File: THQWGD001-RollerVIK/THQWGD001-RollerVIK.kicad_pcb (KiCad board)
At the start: 2 copper layers, 32.1 x 32.1 mm, 9 parts, among them J1 vik-module-connector, J2 Conn_01x02, J3 Conn_01x03

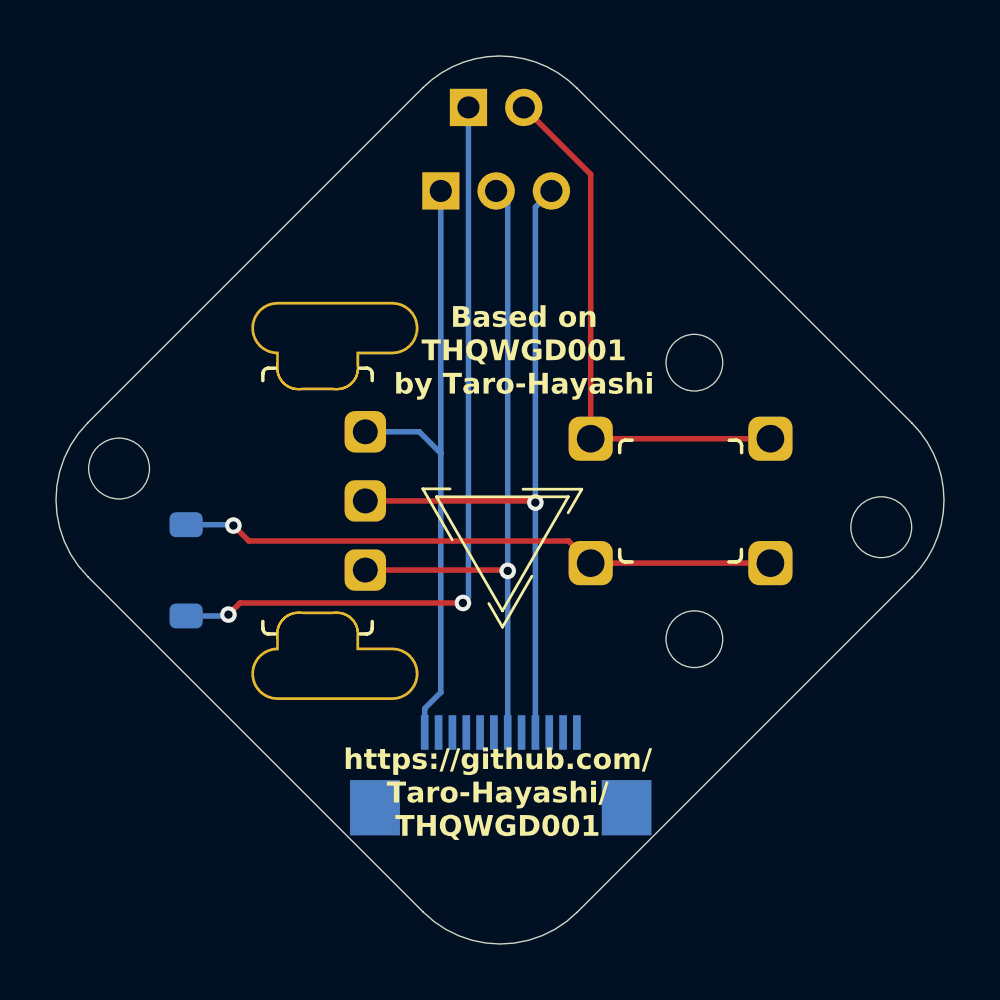
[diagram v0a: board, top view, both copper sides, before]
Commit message: Adjusted the diode placement
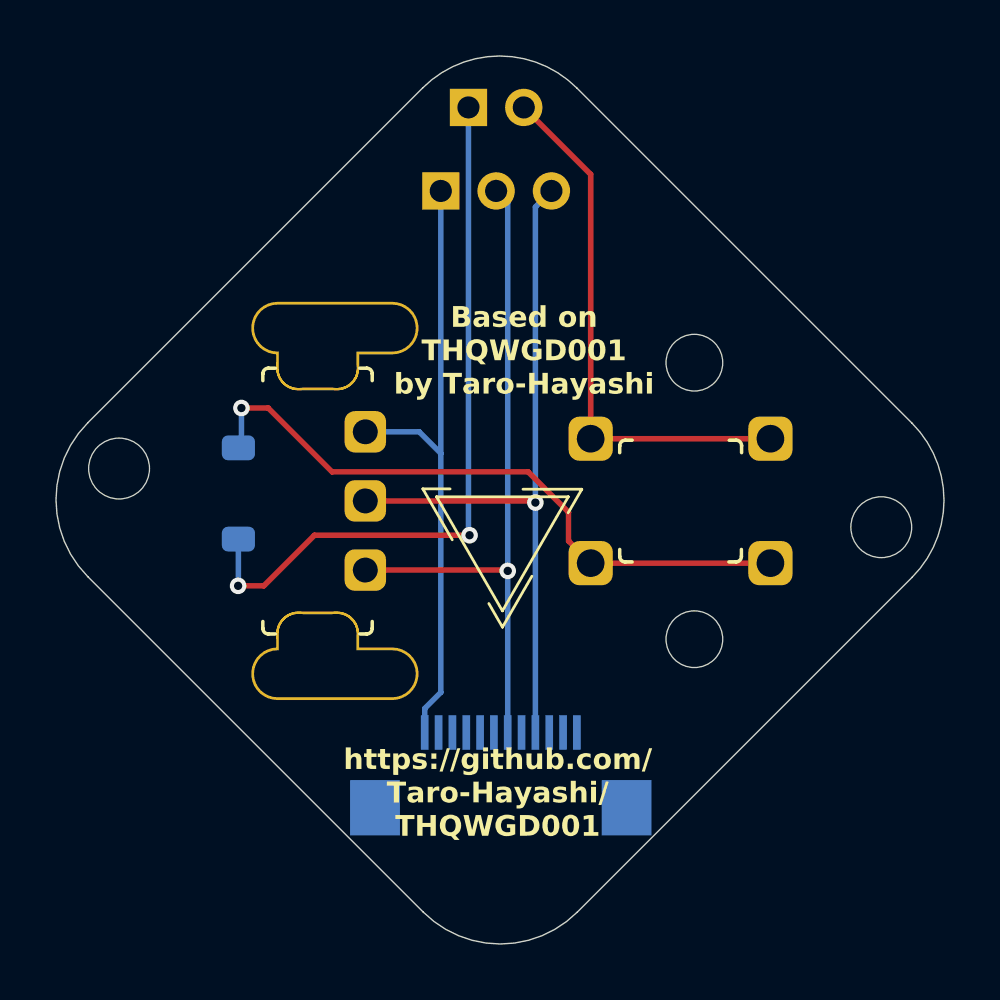
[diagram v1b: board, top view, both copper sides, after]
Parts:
- moved D1 3.36 mm to (116.9, 83.8)
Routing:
- net ROW: track 28.2 -> 26.3 mm
- net Net-(D1-A): track 21.7 -> 23.5 mm
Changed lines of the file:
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@@
 			(fill no)
 			(layer "Cmts.User")
-			(net 11)
 		)
 		(fp_circle
@@
 			(fill no)
 			(layer "F.CrtYd")
-			(net 11)
 		)
 		(fp_text user "${REFERENCE}"
@@
 			(fill no)
 			(layer "Cmts.User")
-			(net 11)
 		)
 		(fp_circle
@@
 			(fill no)
 			(layer "F.CrtYd")
-			(net 11)
 		)
 		(fp_text user "${REFERENCE}"
@@
 	(footprint "Diode_SMD:D_SOD-123"
 		(layer "B.Cu")
-		(at 115.02 86.53 90)
+		(at 116.91 83.75 90)
 		(descr "SOD-123")
 		(tags "SOD-123")
@@
 	)
 	(segment
-		(start 116.55 88.13)
-		(end 116.97 87.71)
+		(start 117.83 87.09)
+		(end 119.66 85.26)
 		(width 0.2)
 		(layer "F.Cu")
@@
 	)
 	(segment
-		(start 116.97 87.71)
-		(end 125.03 87.71)
+		(start 116.9 87.09)
+		(end 117.83 87.09)
 		(width 0.2)
 		(layer "F.Cu")
 		(net 1)
 	)
+	(segment
+		(start 119.66 85.26)
+		(end 125.27 85.26)
+		(width 0.2)
+		(layer "F.Cu")
+		(net 1)
+	)
 	(via
-		(at 116.55 88.13)
+		(at 116.9 87.09)
 		(size 0.6)
 		(drill 0.3)
@@
 	)
 	(via
-		(at 125.03 87.71)
+		(at 125.27 85.26)
 		(size 0.6)
 		(drill 0.3)
@@
 	)
 	(segment
-		(start 125.23 87.51)
-		(end 125.23 69.79)
+		(start 116.91 87.08)
+		(end 116.91 85.4)
 		(width 0.2)
 		(layer "B.Cu")
@@
 	)
 	(segment
-		(start 116.5 88.18)
-		(end 116.55 88.13)
+		(start 125.23 85.22)
+		(end 125.27 85.26)
 		(width 0.2)
 		(layer "B.Cu")
@@
 	)
 	(segment
-		(start 125.03 87.71)
-		(end 125.23 87.51)
+		(start 116.9 87.09)
+		(end 116.91 87.08)
 		(width 0.2)
 		(layer "B.Cu")
@@
 	)
 	(segment
-		(start 115.02 88.18)
-		(end 116.5 88.18)
+		(start 125.23 69.79)
+		(end 125.23 85.22)
 		(width 0.2)
 		(layer "B.Cu")
 		(net 1)
+	)
+	(segment
+		(start 117.99 80.66)
+		(end 120.299 82.969)
+		(width 0.2)
+		(layer "F.Cu")
+		(net 2)
 	)
 	(segment
@@
 	)
 	(segment
+		(start 120.299 82.969)
+		(end 127.388943 82.969)
+		(width 0.2)
+		(layer "F.Cu")
+		(net 2)
+	)
+	(segment
+		(start 117.02 80.66)
+		(end 117.99 80.66)
+		(width 0.2)
+		(layer "F.Cu")
+		(net 2)
+	)
+	(segment
 		(start 128.849 85.469)
 		(end 129.65 86.27)
@@
 	)
 	(segment
-		(start 117.289 85.469)
+		(start 127.388943 82.969)
+		(end 128.849 84.429057)
+		(width 0.2)
+		(layer "F.Cu")
+		(net 2)
+	)
+	(segment
+		(start 128.849 84.429057)
 		(end 128.849 85.469)
 		(width 0.2)
@@
 		(net 2)
 	)
-	(segment
-		(start 116.73 84.91)
-		(end 117.289 85.469)
-		(width 0.2)
-		(layer "F.Cu")
-		(net 2)
-	)
 	(via
-		(at 116.73 84.91)
+		(at 117.02 80.66)
 		(size 0.6)
 		(drill 0.3)
@@
 	)
 	(segment
-		(start 116.7 84.88)
-		(end 116.73 84.91)
+		(start 117.02 80.66)
+		(end 117.02 81.99)
 		(width 0.2)
 		(layer "B.Cu")
@@
 	)
 	(segment
-		(start 115.02 84.88)
-		(end 116.7 84.88)
+		(start 117.02 81.99)
+		(end 116.91 82.1)
 		(width 0.2)
 		(layer "B.Cu")
